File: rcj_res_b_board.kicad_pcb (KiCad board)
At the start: 2 copper layers, 90 x 100 mm, 108 parts, among them P1 GP2Y0A41SK0F, P10 SERVO0, P11 MPU9250, P12 PING0, P13 CONN_01X03, P14 CONN_01X03, P15 CONN_01X04, P16 CONN_01X04, P17 CONN_01X04, P18 CONN_01X04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

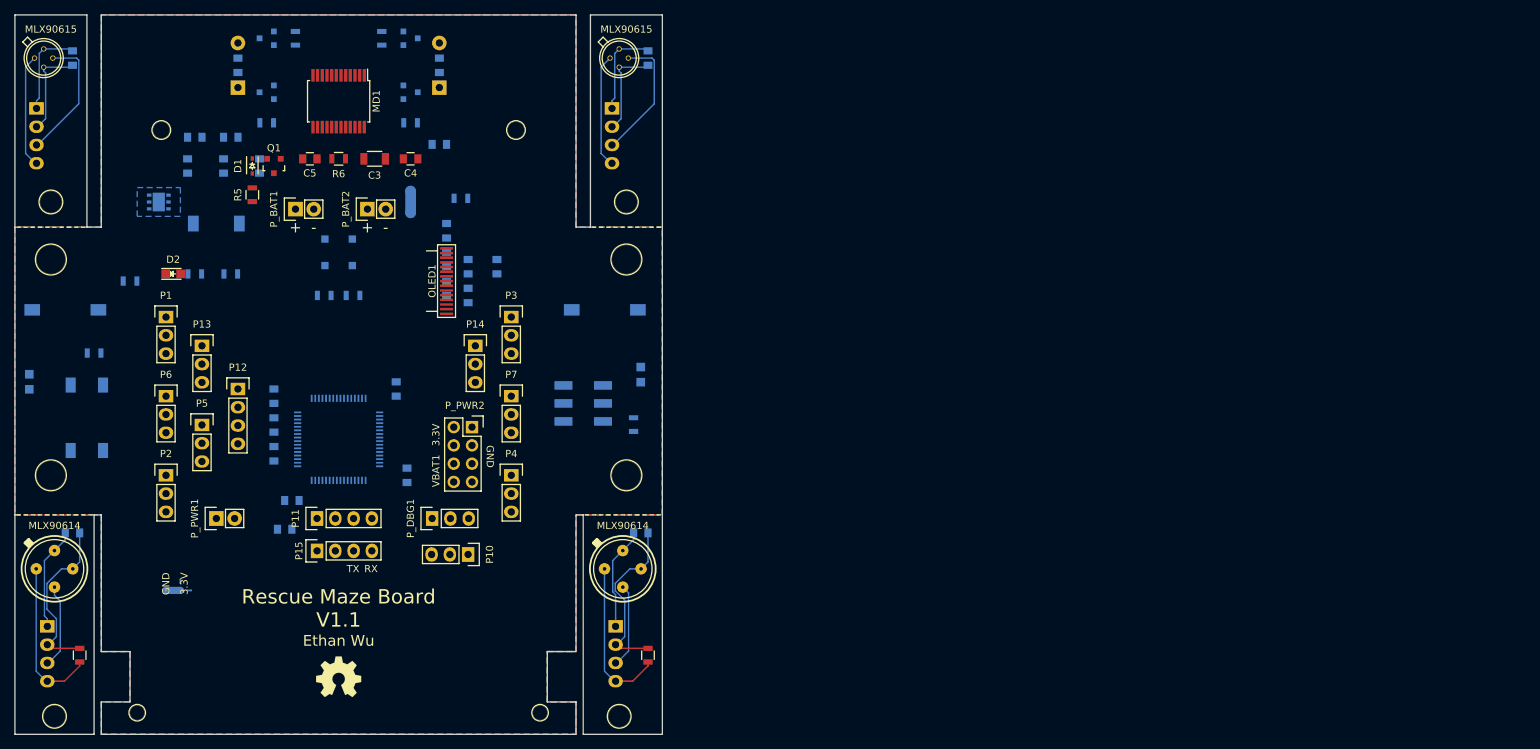
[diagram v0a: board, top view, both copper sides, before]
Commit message: Moved OLED to cut-off board
Removed PIR cutoffs (no longer needed)
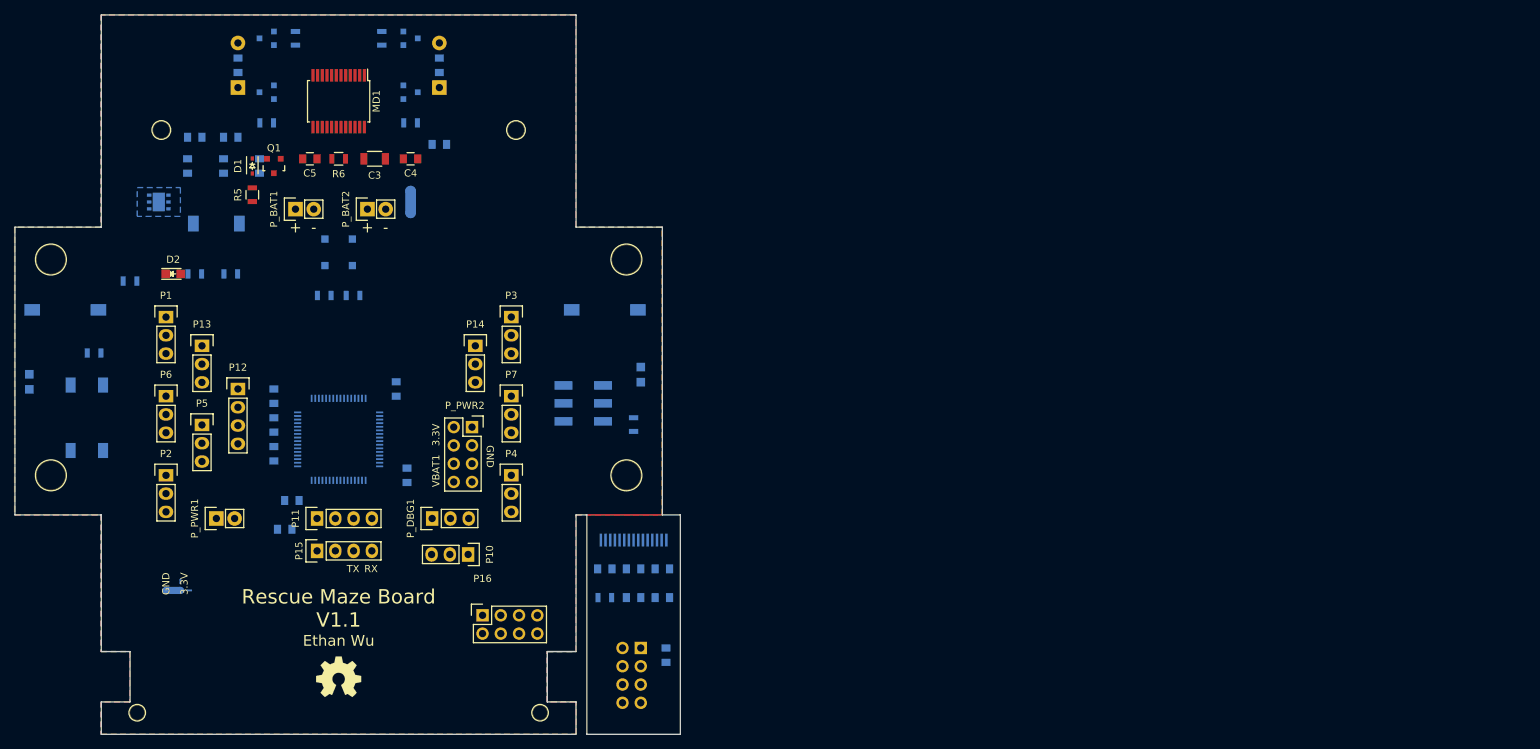
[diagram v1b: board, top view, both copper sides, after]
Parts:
- removed C_CT0_1, C_CT0_2, C_CT0_3, C_CT0_4: 0.1uF, Capacitors_SMD:C_0805
- removed the HOLE7 at (104.0, 147.5)
- removed the HOLE7 at (25.5, 147.5)
- removed the HOLE8 at (25.0, 76.0)
- removed HOLE9: 1pin, Connect:1pin
- removed P17, P18, P19: CONN_01X04, Socket_Strips:Socket_Strip_Straight_1x04
- removed R_CT0_1, R_CT0_2: 10k, Resistors_SMD:R_0805
- removed U_CT0_1, U_CT0_2: MLX90614, Custom:TO-39
- removed U_CT0_3, U_CT0_4: MLX90615, Custom:TO-46_4Pin
- added P_CT1: CONN_02X04, Pin_Headers:Pin_Header_Straight_2x04, B.Cu at (107.0, 138.0)
- OLED1: moved to B.Cu
- P16: value CONN_01X04 -> CONN_02X04; footprint Socket_Strips:Socket_Strip_Straight_1x04 -> Socket_Strips:Socket_Strip_Straight_2x04; moved to F.Cu
- moved P16 60.5 mm to (85.0, 133.5), turned to 0 degrees
- moved R10 59.0 mm to (102.0, 131.0)
- moved C13 58.9 mm to (110.5, 139.0)
- moved C12 53.7 mm to (106.0, 131.0), turned to 0 degrees
- moved C11 52.4 mm to (110.0, 131.0), turned to 0 degrees
- moved C9 51.9 mm to (102.0, 127.0), turned to 0 degrees
- moved C8 47.9 mm to (106.0, 127.0), turned to 180 degrees
- moved C7 46.6 mm to (110.0, 127.0), turned to 180 degrees
- moved OLED1 44.4 mm to (106.0, 123.0), turned to 270 degrees
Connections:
- C11 pad 2: GNDD -> /OLED_Circuitry/GND
- C12 pad 1: /3.3V -> /OLED_Circuitry/3.3V
- C12 pad 2: GNDD -> /OLED_Circuitry/GND
- C13 pad 1: /3.3V -> /OLED_Circuitry/3.3V
- C13 pad 2: GNDD -> /OLED_Circuitry/GND
- C9 pad 2: GNDD -> /OLED_Circuitry/GND
- MCU1 pad 55: /OLED_SCLK -> /SCLK
- MCU1 pad 57: /OLED_MOSI -> /MOSI
- OLED1 pad 10: /OLED_D-C -> /OLED_Circuitry/D-C
- OLED1 pad 11: /OLED_SCLK -> /OLED_Circuitry/SCLK
- OLED1 pad 12: /OLED_MOSI -> /OLED_Circuitry/MOSI
- OLED1 pad 5: /3.3V -> /OLED_Circuitry/3.3V
- OLED1 pad 6: GNDD -> /OLED_Circuitry/GND
- OLED1 pad 7: /3.3V -> /OLED_Circuitry/3.3V
- OLED1 pad 8: /OLED_SS -> /OLED_Circuitry/SS
- OLED1 pad 9: /OLED_RST -> /OLED_Circuitry/RST
- P16 pad 1: Net-(C_CT0_1-Pad2) -> GNDD
- P16 pad 2: Net-(C_CT0_1-Pad1) -> /3.3V
- P16 pad 3: Net-(P16-Pad3) -> /SCLK
- P16 pad 4: Net-(P16-Pad4) -> /MOSI
- R10 pad 1: GNDD -> /OLED_Circuitry/GND
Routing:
- net Net-(C_CT0_2-Pad1): track 24.2 -> 0.00 mm
- net Net-(C_CT0_1-Pad1): track 24.2 -> 0.00 mm
- net Net-(P16-Pad4): track 22.4 -> 0.00 mm
- net Net-(P17-Pad4): track 22.3 -> 0.00 mm
- net (no net): track 0.00 -> 21.0 mm
- net Net-(P19-Pad3): track 18.0 -> 0.00 mm
- net Net-(P18-Pad3): track 18.0 -> 0.00 mm
- net Net-(P18-Pad4): track 15.9 -> 0.00 mm
- net Net-(P19-Pad4): track 15.9 -> 0.00 mm
- net Net-(C_CT0_1-Pad2): track 14.4 -> 0.00 mm
- net Net-(C_CT0_2-Pad2): track 14.4 -> 0.00 mm
- net Net-(C_CT0_4-Pad1): track 13.1 -> 0.00 mm
- net Net-(C_CT0_3-Pad1): track 13.1 -> 0.00 mm
- net Net-(C_CT0_4-Pad2): track 12.8 -> 0.00 mm
- net Net-(C_CT0_3-Pad2): track 12.8 -> 0.00 mm
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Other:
- board size 90 x 100 mm -> 92.5 x 100 mm
- board text removed: "0.1uF"
- board text removed: "MLX90614"
- board text removed: "MLX90615"
- board text removed: "SCL"
- board text removed: "SDA"
- board text removed: "VCC"

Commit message: Initial routing
Added solder bridges
Added missing library
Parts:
- added SB1: 0, Resistors_SMD:R_0805, F.Cu at (70.0, 81.0)
- added SB2: 0, Resistors_SMD:R_0805, F.Cu at (65.0, 79.0)
- NT1: moved to F.Cu
- moved P16 49.3 mm to (76.0, 85.0)
- moved C4 10.5 mm to (64.5, 71.0), turned to 270 degrees
- moved R5 9.22 mm to (55.0, 66.0), turned to 0 degrees
- moved R6 8.54 mm to (73.0, 67.0), turned to 270 degrees
- moved C10 6.00 mm to (51.0, 67.0), turned to 180 degrees
- moved R3 5.66 mm to (59.0, 61.0), turned to 270 degrees
- moved R4 5.66 mm to (71.0, 61.0), turned to 90 degrees
- moved C14 4.12 mm to (49.0, 71.0), turned to 90 degrees
- moved C15 4.00 mm to (45.0, 71.0)
- moved C16 4.00 mm to (40.0, 71.0), turned to 0 degrees
- moved NT1 1.58 mm to (74.5, 74.5)
- moved C3 1.41 mm to (71.0, 71.0), turned to 270 degrees
- moved C5 1.12 mm to (60.5, 71.0), turned to 270 degrees
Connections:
- P_BAT1 pad 2: Net-(C10-Pad1) -> Net-(P_BAT1-Pad2)
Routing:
- net GNDPWR: track 0.00 -> 53.0 mm
- net GND: track 0.00 -> 39.9 mm
- net Net-(C2-Pad2): track 0.00 -> 31.0 mm
- net Net-(C4-Pad1): track 0.00 -> 26.8 mm
- net Net-(C10-Pad1): track 0.00 -> 26.2 mm
- net Net-(C1-Pad1): track 0.00 -> 20.5 mm
- net Net-(C1-Pad2): track 0.00 -> 19.7 mm
- net Net-(C2-Pad1): track 0.00 -> 17.7 mm
- net Net-(C14-Pad1): track 0.00 -> 16.1 mm
- net GNDD: track 0.00 -> 15.3 mm
- net Net-(D1-Pad2): track 0.00 -> 13.1 mm
- net /VBAT1: track 0.00 -> 12.8 mm
- net Net-(P_BAT1-Pad2): track 0.00 -> 10.4 mm
- net /3.3V: track 0.00 -> 7.54 mm
- net VCC: track 0.00 -> 6.24 mm
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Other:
- net class DH_PWR added: clearance 0.5, trace_width 1, via_dia 1.8, via_drill 1.3

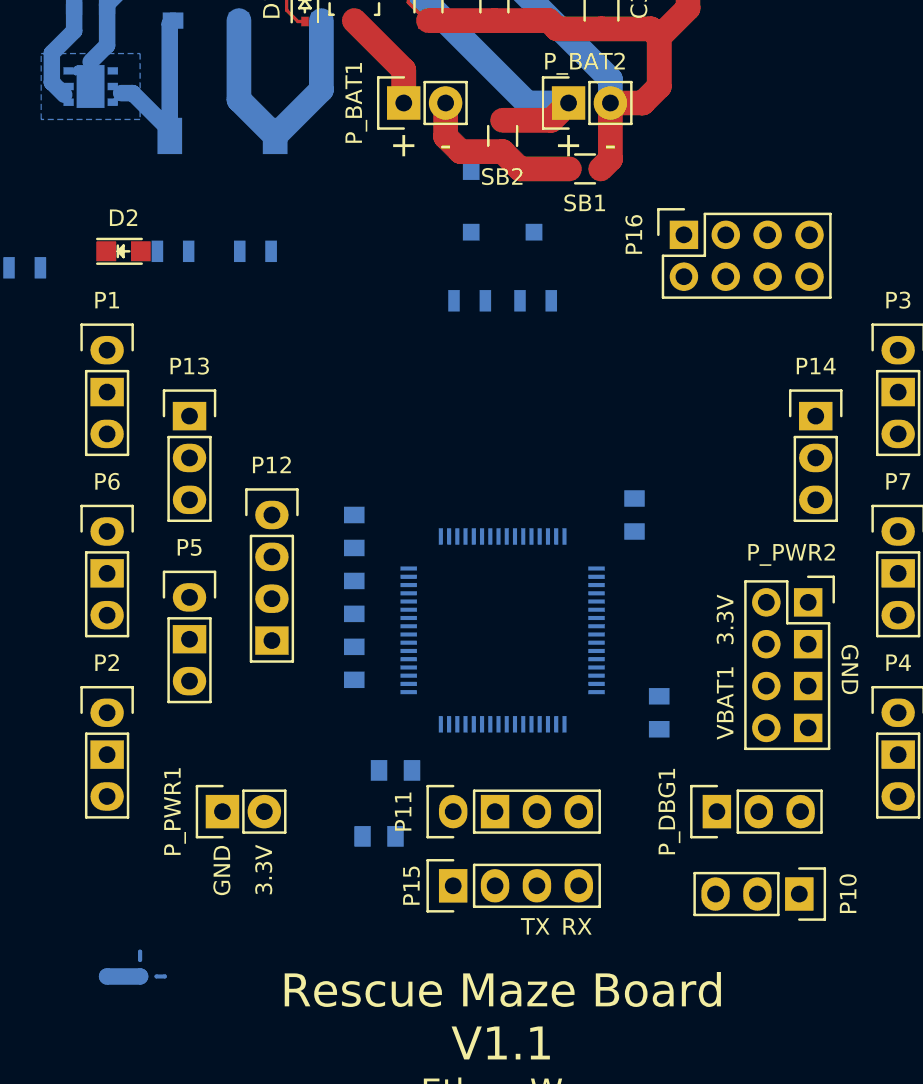
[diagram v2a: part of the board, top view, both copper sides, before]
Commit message: Changed servo to use VBAT power
Also increased size of net-ties
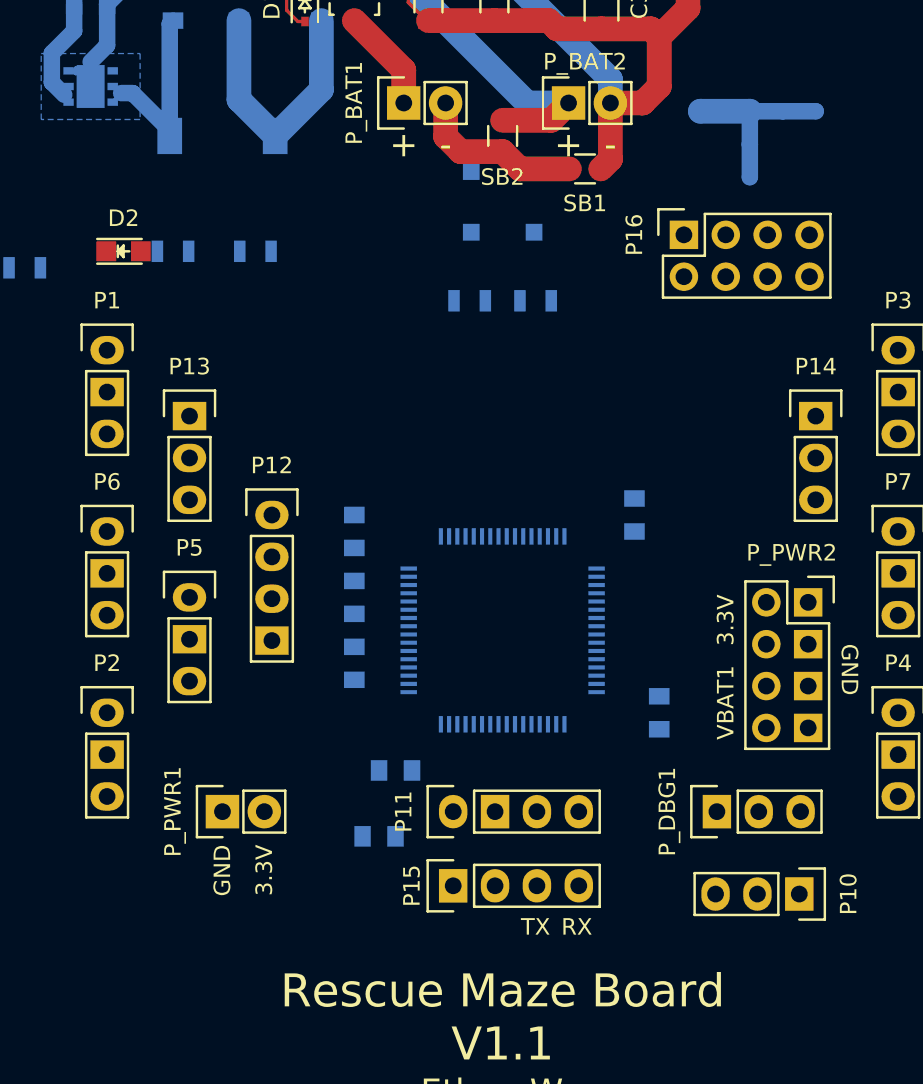
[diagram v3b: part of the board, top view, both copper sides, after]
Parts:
- NT2: footprint Net_Ties:NET_TIE_1mm -> Net_Ties:NET_TIE_1.5mm
- NT3, NT4: footprint Net_Ties:NET_TIE_.25mm -> Net_Ties:NET_TIE_1mm
- moved NT3 65.3 mm to (83.0, 77.5)
- moved NT2 63.9 mm to (78.5, 77.5)
- moved NT4 60.8 mm to (80.0, 80.5), turned to 270 degrees
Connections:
- P10 pad 2: /3.3V -> /VBAT1
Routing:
- net Net-(NT2-Pad2): track 0.00 -> 4.00 mm
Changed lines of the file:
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@@
   (general
     (links 228)
-    (no_connects 176)
-    (area 18.825 28.15 230.000001 188.100001)
+    (no_connects 174)
+    (area 19.924999 49.924999 112.575001 150.100001)
     (thickness 1.6)
     (drawings 51)
-    (tracks 161)
+    (tracks 163)
     (zones 0)
     (modules 94)
@@
     (uvia_drill 0.5)
     (add_net /VBAT1)
+    (add_net "Net-(NT2-Pad2)")
   )
   (net_class D_PWR ""
@@
     (add_net GNDA)
     (add_net GNDD)
-    (add_net "Net-(NT2-Pad2)")
   )
   (net_class MAIN_PWR ""
@@
       (net 38 GNDPWR))
     (pad 2 thru_hole oval (at 2.54 0 180) (size 1.7272 2.032) (drill 1.016) (layers *.Cu *.Mask F.SilkS)
-      (net 3 /3.3V))
+      (net 71 /VBAT1))
     (pad 3 thru_hole oval (at 5.08 0 180) (size 1.7272 2.032) (drill 1.016) (layers *.Cu *.Mask F.SilkS)
       (net 39 /SERVO0_PWM))
@@
       (net 32 GND))
   )
-  (module Net_Ties:NET_TIE_1mm (layer B.Cu)
-    (at 42 130)
-    (fp_text reference NT2 (at 0 -1.25) (layer B.SilkS) hide
-      (effects (font (size 1 1) (thickness 0.15)) (justify mirror))
-    )
-    (fp_text value Net_Tie (at 0 1.25) (layer B.Fab)
-      (effects (font (size 1 1) (thickness 0.15)) (justify mirror))
-    )
-    (fp_line (start -1 0) (end 1 0) (layer B.Cu) (width 1))
-    (pad 1 connect oval (at -1 0) (size 1 1) (layers B.Cu)
-      (net 32 GND))
-    (pad 2 connect oval (at 1 0) (size 1 1) (layers B.Cu)
-      (net 55 "Net-(NT2-Pad2)"))
-  )
-  (module Net_Ties:NET_TIE_.25mm (layer B.Cu)
-    (at 44.25 130)
-    (fp_text reference NT3 (at 0 -1) (layer B.SilkS) hide
-      (effects (font (size 1 1) (thickness 0.15)) (justify mirror))
-    )
-    (fp_text value Net_Tie (at 0 1) (layer B.Fab)
-      (effects (font (size 1 1) (thickness 0.15)) (justify mirror))
-    )
-    (fp_line (start -0.25 0) (end 0.25 0) (layer B.Cu) (width 0.25))
-    (pad 1 connect oval (at -0.25 0) (size 0.25 0.25) (layers B.Cu)
-      (net 55 "Net-(NT2-Pad2)"))
-    (pad 2 connect oval (at 0.25 0) (size 0.25 0.25) (layers B.Cu)
-      (net 2 GNDD))
-  )
-  (module Net_Ties:NET_TIE_.25mm (layer B.Cu)
-    (at 43 128.75 90)
-    (fp_text reference NT4 (at 0 -1 90) (layer B.SilkS) hide
-      (effects (font (size 1 1) (thickness 0.15)) (justify mirror))
-    )
-    (fp_text value Net_Tie (at 0 1 90) (layer B.Fab)
-      (effects (font (size 1 1) (thickness 0.15)) (justify mirror))
-    )
-    (fp_line (start -0.25 0) (end 0.25 0) (layer B.Cu) (width 0.25))
-    (pad 1 connect oval (at -0.25 0 90) (size 0.25 0.25) (layers B.Cu)
-      (net 55 "Net-(NT2-Pad2)"))
-    (pad 2 connect oval (at 0.25 0 90) (size 0.25 0.25) (layers B.Cu)
-      (net 5 GNDA))
-  )
   (module Custom:JS202011SCQN (layer B.Cu)
     (at 99 104)
@@
     )
   )
+  (module Net_Ties:NET_TIE_1.5mm (layer B.Cu)
+    (at 78.5 77.5)
+    (fp_text reference NT2 (at 0 -2) (layer B.SilkS) hide
+      (effects (font (size 1 1) (thickness 0.15)) (justify mirror))
+    )
+    (fp_text value Net_Tie (at 0 2) (layer B.Fab)
+      (effects (font (size 1 1) (thickness 0.15)) (justify mirror))
+    )
+    (fp_line (start -1.5 0) (end 1.5 0) (layer B.Cu) (width 1.5))
+    (pad 2 connect oval (at 1.5 0) (size 1.5 1.5) (layers B.Cu)
+      (net 55 "Net-(NT2-Pad2)"))
+    (pad 1 connect oval (at -1.5 0) (size 1.5 1.5) (layers B.Cu)
+      (net 32 GND))
+  )
+  (module Net_Ties:NET_TIE_1mm (layer B.Cu)
+    (at 83 77.5)
+    (fp_text reference NT3 (at 0 -1.25) (layer B.SilkS) hide
+      (effects (font (size 1 1) (thickness 0.15)) (justify mirror))
+    )
+    (fp_text value Net_Tie (at 0 1.25) (layer B.Fab)
+      (effects (font (size 1 1) (thickness 0.15)) (justify mirror))
+    )
+    (fp_line (start -1 0) (end 1 0) (layer B.Cu) (width 1))
+    (pad 1 connect oval (at -1 0) (size 1 1) (layers B.Cu)
+      (net 55 "Net-(NT2-Pad2)"))
+    (pad 2 connect oval (at 1 0) (size 1 1) (layers B.Cu)
+      (net 2 GNDD))
+  )
+  (module Net_Ties:NET_TIE_1mm (layer B.Cu)
+    (at 80 80.5 270)
+    (fp_text reference NT4 (at 0 -1.25 270) (layer B.SilkS) hide
+      (effects (font (size 1 1) (thickness 0.15)) (justify mirror))
+    )
+    (fp_text value Net_Tie (at 0 1.25 270) (layer B.Fab)
+      (effects (font (size 1 1) (thickness 0.15)) (justify mirror))
+    )
+    (fp_line (start -1 0) (end 1 0) (layer B.Cu) (width 1))
+    (pad 1 connect oval (at -1 0 270) (size 1 1) (layers B.Cu)
+      (net 55 "Net-(NT2-Pad2)"))
+    (pad 2 connect oval (at 1 0 270) (size 1 1) (layers B.Cu)
+      (net 5 GNDA))
+  )
   (gr_line (start 99.5 150) (end 99.5 119.5) (layer Edge.Cuts) (width 0.15))
   (gr_line (start 112.5 150) (end 99.5 150) (layer Edge.Cuts) (width 0.15))
@@
   (segment (start 76.25 66.049998) (end 70.725003 60.525001) (width 1.5) (layer F.Cu) (net 38))
   (segment (start 60.5 72) (end 64.5 72) (width 1.5) (layer F.Cu) (net 38))
+  (segment (start 80 79.5) (end 80 77.5) (width 1) (layer B.Cu) (net 55))
+  (segment (start 80 77.5) (end 82 77.5) (width 1) (layer B.Cu) (net 55))
   (segment (start 68.260667 58.760667) (end 68.260667 58.714333) (width 0.2) (layer F.Cu) (net 59))
   (segment (start 68.260667 58.714333) (end 68.575 58.4) (width 0.2) (layer F.Cu) (net 59))

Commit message: More preliminary routing
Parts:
- NT2, NT3, NT4: moved to F.Cu
- moved R5 7.28 mm to (57.0, 73.0)
- moved C21 6.32 mm to (67.0, 100.0), turned to 180 degrees
- moved NT3 4.72 mm to (79.0, 80.0), turned to 270 degrees
- moved D1 4.47 mm to (57.0, 69.0)
- moved Q1 2.83 mm to (54.0, 69.0), turned to 90 degrees
- moved NT4 2.69 mm to (81.0, 78.0)
- moved NT2 1.12 mm to (77.5, 77.0)
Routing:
- net /3.3V: track 7.54 -> 299.6 mm, vias 0 -> 2
- net GNDD: track 15.3 -> 269.4 mm, vias 0 -> 2
- net GNDA: track 0.00 -> 142.8 mm, vias 0 -> 1
- net GNDPWR: track 53.0 -> 127.5 mm
- net Net-(D1-Pad2): track 13.1 -> 5.85 mm
- net /MD_BPWM: track 0.00 -> 6.36 mm
- net /MD_APWM: track 0.00 -> 6.36 mm
- net VCC: track 6.24 -> 12.0 mm
- net Net-(R9-Pad2): track 0.00 -> 5.01 mm
- net GND: track 39.9 -> 44.3 mm
- net Net-(C23-Pad1): track 0.00 -> 4.11 mm
- net Net-(C4-Pad1): track 26.8 -> 30.3 mm
- net Net-(C21-Pad1): track 0.00 -> 3.40 mm
- added copper zone on B.Cu, net (none)
- added copper zone on F.Cu, net (none)
- removed copper zone on F.Cu, net GNDD
